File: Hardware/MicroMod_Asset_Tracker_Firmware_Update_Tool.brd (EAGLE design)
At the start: 22 x 22 mm, 36 parts, among them J5 MICROMOD-2222, U2 CH340G, Y1 12MHz

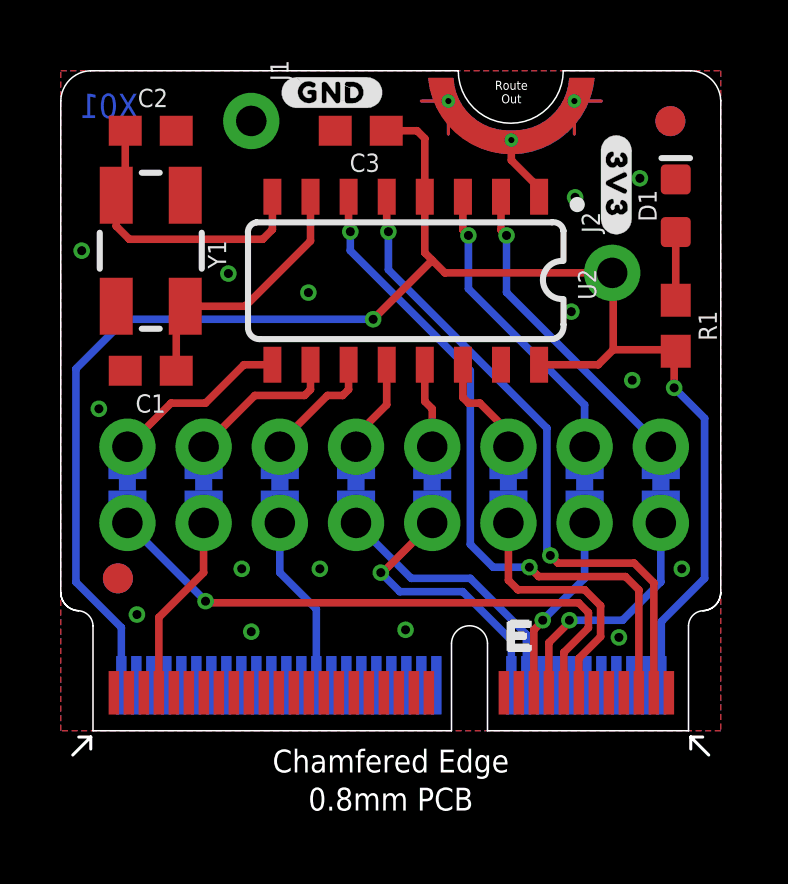
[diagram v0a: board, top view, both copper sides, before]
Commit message: Adding production panel (8x2)
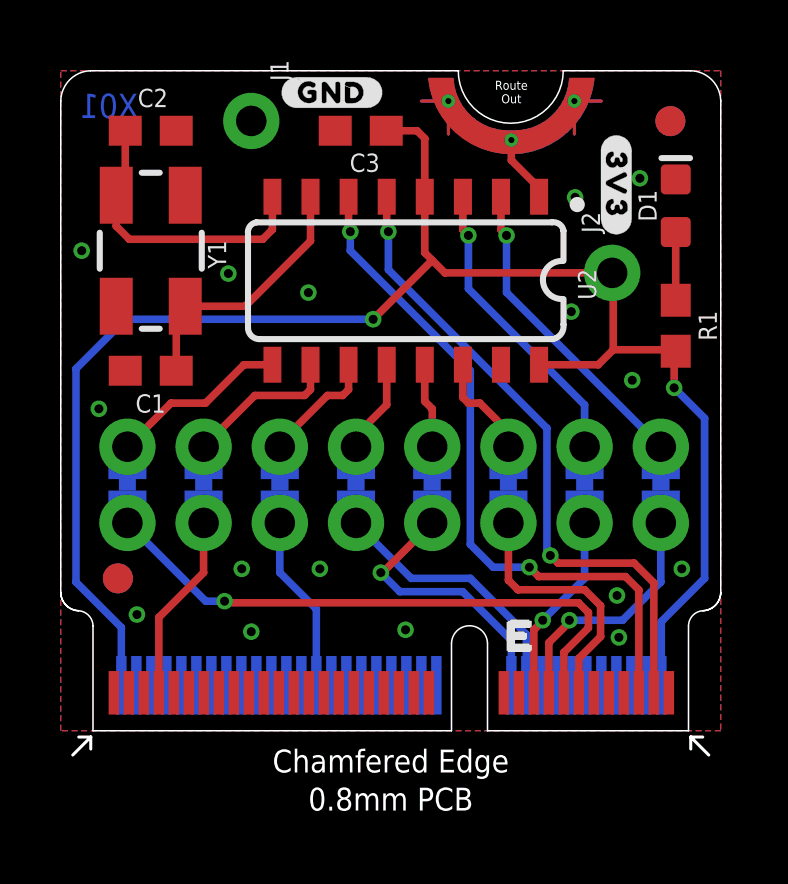
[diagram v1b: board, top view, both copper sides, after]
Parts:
- added U$6: (no value), output:#3V3#3
- added U$7: (no value), output:#GND#2
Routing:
- net GND: vias 15 -> 16
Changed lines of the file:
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@@
 <element name="U$5" library="output" package="#RI#0" value="" x="7.3025" y="11.8745" smashed="yes" rot="MR90"/>
 <element name="LOGO2" library="SparkFun-Aesthetics" package="ORDERING_INSTRUCTIONS" value="SPECIAL_INSTRUCTIONS-ORDERING" x="27.94" y="44.45" smashed="yes"/>
+<element name="U$6" library="output" package="#3V3#3" value="" x="18.502" y="18.1885" smashed="yes" rot="MR90"/>
+<element name="U$7" library="output" package="#GND#2" value="" x="9.04" y="21.272" smashed="yes" rot="MR0"/>
 </elements>
 <signals>
@@
 <via x="6.0325" y="5.3975" extent="1-16" drill="0.3"/>
 <via x="8.636" y="5.3975" extent="1-16" drill="0.3"/>
+<via x="18.542" y="4.5085" extent="1-16" drill="0.3"/>
 </signal>
 <signal name="3.3V" class="1">
@@
 <wire x1="16.77" y1="1.265" x2="16.77" y2="2.6095" width="0.254" layer="1"/>
 <wire x1="16.77" y1="2.6095" x2="17.5895" y2="3.429" width="0.254" layer="1"/>
-<wire x1="4.8792" y1="4.2648" x2="4.826" y2="4.318" width="0.254" layer="1"/>
-<via x="4.826" y="4.318" extent="1-16" drill="0.3"/>
-<wire x1="4.826" y1="4.318" x2="4.826" y2="4.324" width="0.254" layer="16"/>
-<wire x1="4.826" y1="4.324" x2="2.2225" y2="6.9275" width="0.254" layer="16"/>
+<wire x1="5.5142" y1="4.2648" x2="5.461" y2="4.318" width="0.254" layer="1"/>
+<via x="5.461" y="4.318" extent="1-16" drill="0.3"/>
+<wire x1="5.461" y1="4.318" x2="4.832" y2="4.318" width="0.254" layer="16"/>
+<wire x1="4.832" y1="4.318" x2="2.2225" y2="6.9275" width="0.254" layer="16"/>
 <wire x1="17.5895" y1="3.429" x2="17.5895" y2="3.937" width="0.254" layer="1"/>
 <wire x1="17.5895" y1="3.937" x2="17.2617" y2="4.2648" width="0.254" layer="1"/>
-<wire x1="17.2617" y1="4.2648" x2="4.8792" y2="4.2648" width="0.254" layer="1"/>
+<wire x1="17.2617" y1="4.2648" x2="5.5142" y2="4.2648" width="0.254" layer="1"/>
 <wire x1="2.2225" y1="6.9275" x2="2.2225" y2="7.6895" width="0.254" layer="16"/>
 </signal>

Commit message: Changed to the CH340C
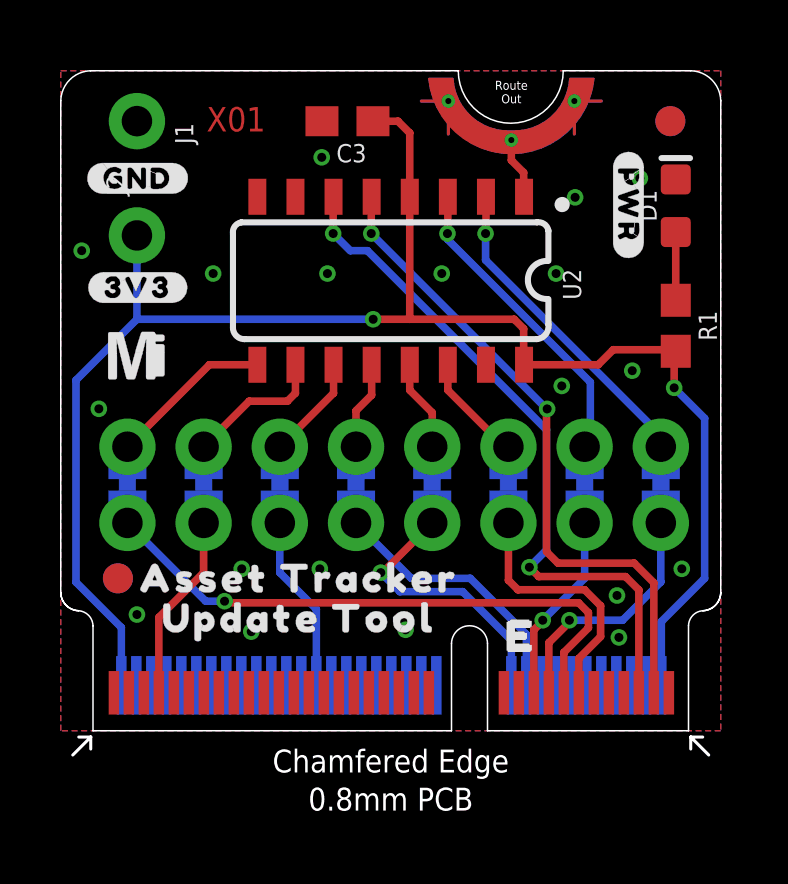
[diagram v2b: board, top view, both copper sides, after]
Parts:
- removed C1, C2: 18pF, SparkFun-Capacitors:0603
- removed Y1: 12MHz, SparkFun-Clocks:CRYSTAL-SMD-5X3.2-4PAD
- added U$10: (no value), output:ASSET_TRACKER0
- added U$11: (no value), output:UPDATE_TOOL0
- added U$8: (no value), output:#PWR#0
- added U$9: (no value), SparkFun-MicroMod:MICROMOD_MI_LOGO_.35
- U2: value CH340G -> CH340C
- moved U$17 16.3 mm to (2.57, 14.8), turned to 0 degrees
- moved U$6 16.3 mm to (2.58, 14.8), turned to 0 degrees
- moved J2 15.9 mm to (2.54, 16.5)
- moved LOGO1 8.52 mm to (11.0, 19.1)
- moved U$3 7.08 mm to (2.56, 18.4)
- moved U$7 7.08 mm to (2.56, 18.4)
- moved J1 3.81 mm to (2.54, 20.3)
- moved C3 0.55 mm to (9.56, 20.3)
- moved U2 0.50 mm to (11.0, 15.0)
- moved SPARKX2 0.41 mm to (11.0, 16.2)
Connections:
- removed net N$1: C2.2, U2.8, Y1.1
- removed net N$2: C1.2, U2.7, Y1.3
- net GND: no longer C1.1, C2.1
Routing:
- net N$1: track 9.92 -> 0.00 mm
- net N$2: track 8.82 -> 0.00 mm
- net !RI!_I: track 4.74 -> 4.24 mm
- net !CTS!_I: track 6.73 -> 6.22 mm
- net GND: track 2.27 -> 2.07 mm, vias 16 -> 19

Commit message: Updates for v10
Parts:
- removed SPARKX2: SPARKX-LOGO4, SparkX:SPARKX-MEDIUM
- added LOGO3: SFE_LOGO_NAME_FLAME.1_INCH, SparkFun-Aesthetics:SFE_LOGO_NAME_FLAME_.1
- added U$12: (no value), SparkFun-MicroMod:MICROMOD_LOGO_.35
- moved LOGO1 8.98 mm to (19.9, 17.8)
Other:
- board text added: "2-Layer PCB 0.8mm Thickness Exposed Edge Gold Fingers 45° Finger Chamfered ENIG Finish"
- board text added: "v10"
- board text removed: "2-Layer PCB 0.8mm Thickness Exposed Edge HASL Finish"
- board text removed: "X01"
